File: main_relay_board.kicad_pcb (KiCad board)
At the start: 4 copper layers, 128.5 x 88.3 mm, 148 parts, among them J101 Screw_Terminal_01x03, J102 Conn_01x04_Socket, J103 Conn_01x04_Socket, J104 Conn_01x08_Socket, J105 Conn_01x04_Socket, J106 Conn_01x04_Socket, J107 Conn_01x06_Socket, J108 Conn_01x04_Socket, J109 Conn_01x04_Socket, J110 Conn_01x04_Socket, J111 Screw_Terminal_01x03, Q401 AO3422, Q402 AO3422, Q403 AO3422, Q601 AO3422, Q602 AO3422, Q603 AO3422, Q604 AO3422, Q605 AO3422, Q606 IPD70R360P7S, Q701 IPD70R360P7S, SW301 RST_SW, U201 AP63205WU, U202 TLV1117-33, U301 STM32F205RBTx, U302 MCP9700x-ETT, U401 STM8S003F3P, U701 LM5168FDDAR, U702 AMC1311QDWVR, U703 TLV9001IDCK, U704 SN74LVC1G14DBV, Y301 Crystal_GND24

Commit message: finished...
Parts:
- removed C709: 2u2, Capacitor_SMD:C_0603_1608Metric
- added D702: DFLS1200-7, Diode_SMD_AKL:D_PowerDI-123, F.Cu at (208.3, 64.0)
- added D703: DFLS1200-7, Diode_SMD_AKL:D_PowerDI-123, F.Cu at (197.1, 59.2)
- added G***: LOGO, LOGO, F.Cu at (181.1, 111.0)
- added REF**: Symbol_HighVoltage_NoTriangle_6x15mm_Copper, Symbol:Symbol_HighVoltage_NoTriangle_6x15mm_Copper, F.Cu at (205.0, 109.9)
- added REF**: KiCad-Logo_5mm_SilkScreen, Symbol:KiCad-Logo_5mm_SilkScreen, F.Cu at (130.7, 46.9)
- added REF**: Symbol_HighVoltage_NoTriangle_2x5mm_Copper, Symbol:Symbol_HighVoltage_NoTriangle_2x5mm_Copper, F.Cu at (191.3, 45.5)
- C701: value 1u -> 220n; footprint Capacitor_SMD:C_1812_4532Metric_Pad1.57x3.40mm_HandSolder -> Capacitor_SMD:C_0603_1608Metric
- C705: value 2n2 -> 10u; footprint Capacitor_SMD:C_0603_1608Metric -> Capacitor_THT:CP_Radial_D10.0mm_P5.00mm
- C706: value 56p -> 100n
- C708: value 1n2 -> 100u; footprint Capacitor_SMD:C_0603_1608Metric -> Capacitor_SMD:C_1206_3216Metric
- L701: value 56u -> 680u; footprint Inductor_SMD:L_1210_3225Metric -> Inductor_SMD:L_12x12mm_H8mm
- R701: value 22k1 -> 10
- R709: value 340k -> 44k2
- R712: value 316k -> 10k
- R713: value 101k -> 11k8; footprint Resistor_SMD:R_0603_1608Metric -> Resistor_SMD_AKL:R_0402_1005Metric
- U701: value LM5168FDDAR -> UCC28881DR; footprint Package_SO:TI_SO-PowerPAD-8 -> footprints:D0007A_N
- Y301: value Crystal_GND24 -> 8MHz
- moved R713 38.8 mm to (201.2, 83.3), turned to 0 degrees
- moved C708 30.3 mm to (200.9, 78.0), turned to 180 degrees
- moved R709 25.1 mm to (212.5, 63.0), turned to -90 degrees
- moved R505 18.3 mm to (124.8, 97.0), turned to -90 degrees
- moved D505 17.4 mm to (124.8, 92.5), turned to 90 degrees
- moved R712 15.3 mm to (208.3, 60.5), turned to 180 degrees
- moved C706 12.9 mm to (191.5, 55.6), turned to -90 degrees
- moved C705 12.8 mm to (207.3, 49.9)
- moved R714 11.8 mm to (177.3, 99.1)
- moved C702 11.2 mm to (202.6, 97.8)
- moved C703 11.2 mm to (201.4, 102.2)
- moved R702 11.2 mm to (210.6, 88.4)
- moved R703 11.2 mm to (208.6, 91.6)
- moved R704 11.2 mm to (210.5, 93.0)
- moved R705 11.2 mm to (208.6, 96.0)
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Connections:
- C701 pad 1: V_MTRCTRL -> Net-(D703-K)
- C701 pad 2: HSGND -> Net-(D702-K)
- C705 pad 1: Net-(U701-BST) -> Net-(U701-DRAIN)
- C705 pad 2: Net-(U701-SW) -> HSGND
- C706 pad 1: Net-(C706-Pad1) -> Net-(D703-K)
- C706 pad 2: Net-(U701-FB) -> Net-(U701-VDD)
- C708 pad 1: Net-(C706-Pad1) -> HSGND
- L701 pad 1: Net-(U701-SW) -> Net-(D703-K)
- R701 pad 1: Net-(U701-RT) -> Net-(U701-DRAIN)
- R701 pad 2: HSGND -> V_MTRCTRL
- R709 pad 1: Net-(U701-SW) -> Net-(U701-FB)
- R709 pad 2: Net-(C706-Pad1) -> Net-(D702-K)
- R712 pad 1: HS+5V -> Net-(U701-FB)
- R712 pad 2: Net-(U701-FB) -> Net-(D703-K)
- R713 pad 1: Net-(U701-FB) -> HS+5V
- U701 pad 1: HSGND -> Net-(D703-K)
- U701 pad 2: V_MTRCTRL -> Net-(D703-K)
- U701 pad 3: V_MTRCTRL -> Net-(U701-FB)
- U701 pad 4: Net-(U701-RT) -> Net-(U701-VDD)
- U701 pad 5: Net-(U701-FB) -> Net-(U701-DRAIN)
- U701 pad 8: Net-(U701-SW) -> Net-(U701-DRAIN)
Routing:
- net Net-(D703-K): track 0.00 -> 39.9 mm
- net Net-(U701-DRAIN): track 0.00 -> 33.4 mm
- net HS+5V: track 80.2 -> 53.9 mm, vias 4 -> 2
- net BMS_OK_FINAL: track 9.98 -> 31.0 mm
- net Net-(U701-SW): track 19.0 -> 0.00 mm
- net Net-(C706-Pad1): track 15.6 -> 0.00 mm
- net Net-(U701-VDD): track 0.00 -> 12.7 mm, vias 0 -> 2
- net V_MTRCTRL: track 67.9 -> 55.8 mm
- net GND: track 188.1 -> 177.1 mm, vias 47 -> 48
- net Net-(D702-K): track 0.00 -> 10.6 mm
- net Net-(U701-BST): track 8.95 -> 0.00 mm
- net VSENSE_OUT: track 46.9 -> 55.9 mm
- net Net-(U701-FB): track 28.6 -> 20.5 mm
- net MCU_OK: track 55.3 -> 63.2 mm
- net Net-(U703-+): track 7.61 -> 13.6 mm
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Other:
- board text added: "BMS_OK"
- board text added: "IMD_OK"
- board text added: "MCU_OK"
- board text added: "PCHRG AUX"
- board text added: "R1"
- board text added: "UBC THUNDERBIKES RELAY CNTRL BOARD"
- board text removed: "ISO_+5V"

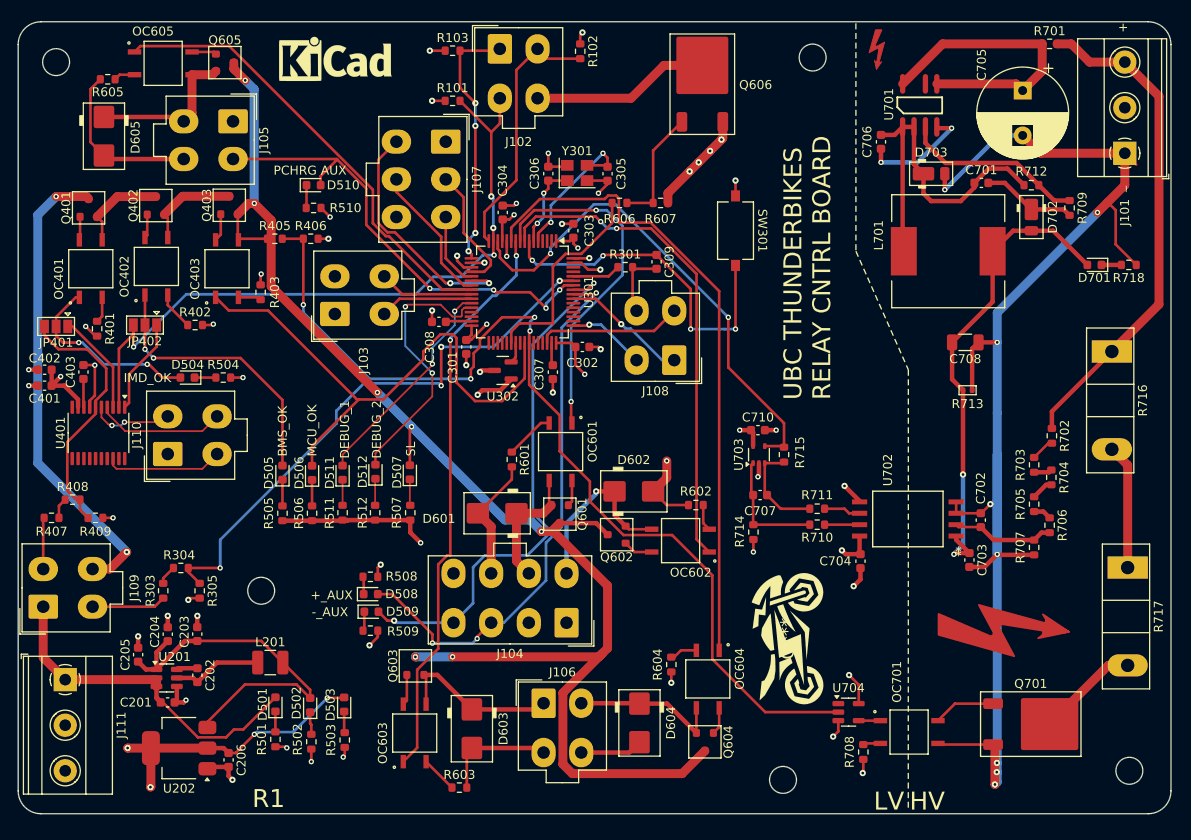
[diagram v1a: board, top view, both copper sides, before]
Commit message: switched to an isolated dcdc transformer from LS 5V
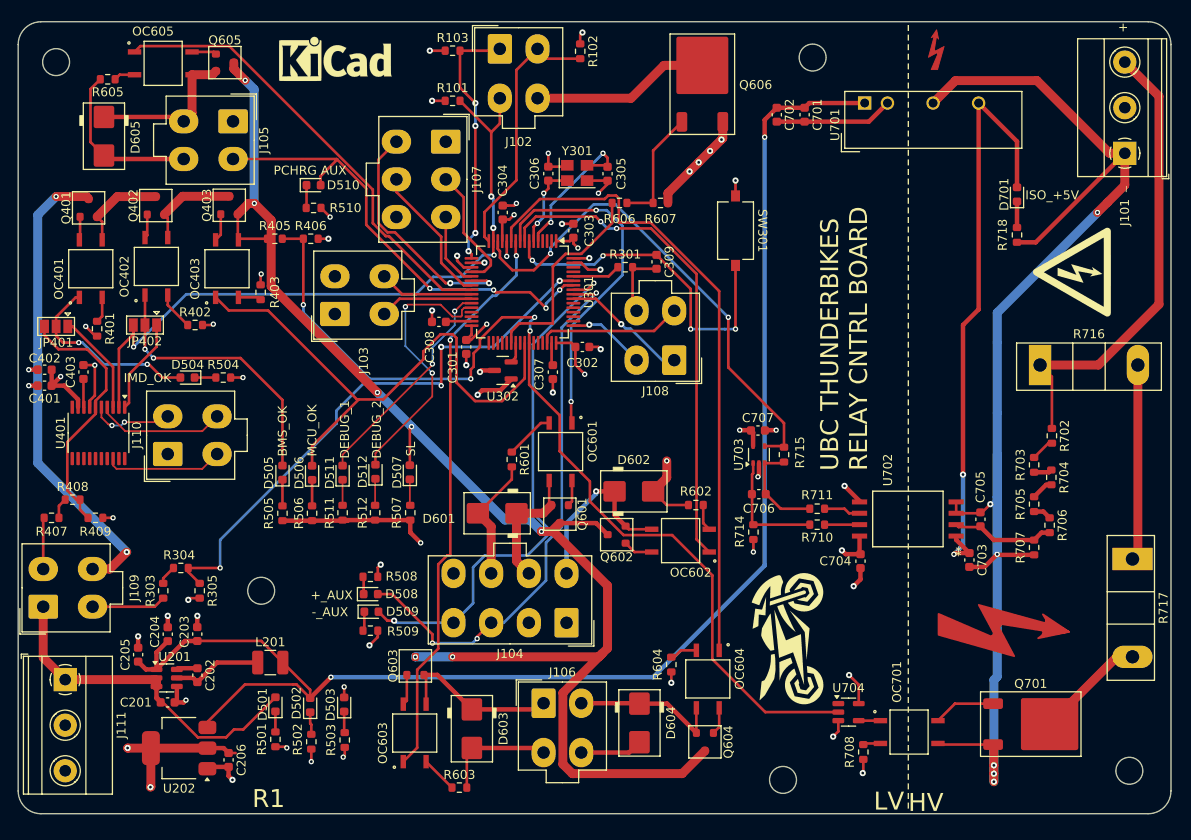
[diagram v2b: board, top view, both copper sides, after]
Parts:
- removed C708: 100u, Capacitor_SMD:C_1206_3216Metric
- removed C710: 100n, Capacitor_SMD:C_0603_1608Metric
- removed D702, D703: DFLS1200-7, Diode_SMD_AKL:D_PowerDI-123
- removed L701: 680u, Inductor_SMD:L_12x12mm_H8mm
- removed R701: 10, Resistor_SMD:R_0603_1608Metric
- removed R709: 44k2, Resistor_SMD:R_0603_1608Metric
- removed R712: 10k, Resistor_SMD:R_0603_1608Metric
- removed R713: 11k8, Resistor_SMD_AKL:R_0402_1005Metric
- added G***: LOGO, LOGO, F.Cu at (212.8, 70.2)
- C701: value 220n -> 4u7
- C702: value 100p -> 4u7
- C705: value 10u -> 100p; footprint Capacitor_THT:CP_Radial_D10.0mm_P5.00mm -> Capacitor_SMD:C_0603_1608Metric
- C706: value 100n -> 100p
- C707: value 100p -> 100n
- U701: value UCC28881DR -> TMA-0505S; footprint footprints:D0007A_N -> Converter_DCDC:Converter_DCDC_TRACO_TMA-05xxS_12xxS_Single_THT
- moved C702 50.6 mm to (179.9, 52.6), turned to -90 degrees
- moved C705 48.0 mm to (202.6, 97.7), turned to 90 degrees
- moved C706 41.6 mm to (177.9, 94.9), turned to 0 degrees
- moved C701 21.1 mm to (183.0, 52.6), turned to -90 degrees
- moved R718 12.9 mm to (206.7, 66.0), turned to -90 degrees
- moved D701 11.7 mm to (206.7, 61.5), turned to 90 degrees
- moved R716 8.14 mm to (209.2, 80.5), turned to 0 degrees
- moved C707 7.20 mm to (177.8, 87.8)
- moved U701 6.14 mm to (189.7, 51.3)
- moved REF** 6.13 mm to (197.4, 45.2), turned to 180 degrees
- moved R717 1.10 mm to (219.6, 102.1)
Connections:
- C701 pad 1: Net-(D703-K) -> +5V
- C701 pad 2: Net-(D702-K) -> GND
- C702 pad 1: Net-(U702-VIN) -> +5V
- C702 pad 2: HSGND -> GND
- C705 pad 1: Net-(U701-DRAIN) -> Net-(U702-VIN)
- C706 pad 1: Net-(D703-K) -> Net-(U703-+)
- C706 pad 2: Net-(U701-VDD) -> Net-(U703--)
- C707 pad 1: Net-(U703-+) -> +3V3
- C707 pad 2: Net-(U703--) -> GND
- U701 pad 1: Net-(D703-K) -> +5V
- U701 pad 2: Net-(D703-K) -> GND
- U701 pad 4: Net-(U701-VDD) -> HSGND
- U701 pad 6: unconnected-(U701-NC-Pad6) -> HS+5V
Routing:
- net +5V: track 42.1 -> 160.5 mm, vias 0 -> 2
- net Net-(D703-K): track 39.9 -> 0.00 mm
- net Net-(U701-DRAIN): track 33.4 -> 0.00 mm
- net Net-(U701-FB): track 20.5 -> 0.00 mm
- net +3V3: track 81.5 -> 68.0 mm, vias 18 -> 17
- net GND: track 177.1 -> 190.3 mm
- net HS+5V: track 53.9 -> 66.9 mm
- net Net-(U701-VDD): track 12.7 -> 0.00 mm, vias 2 -> 0
- net Net-(D702-K): track 10.6 -> 0.00 mm
- net Net-(R716-Pad2): track 13.9 -> 21.9 mm
- net V_MTRCTRL: track 55.8 -> 52.3 mm
- net HSGND: track 155.7 -> 154.2 mm, vias 8 -> 6
- net Net-(Q701-D): track 11.9 -> 12.8 mm
- net Net-(D701-K): track 2.22 -> 2.91 mm
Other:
- board text added: "ISO_+5V"
